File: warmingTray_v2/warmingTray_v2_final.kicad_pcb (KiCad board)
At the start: 2 copper layers, 116.1 x 53.8 mm, 38 parts, among them J1 Jack-DC, P1 Power, P2 Analog, P3 Analog, P4 Digital, P5 PWM, P6 PWM, P7 Communication

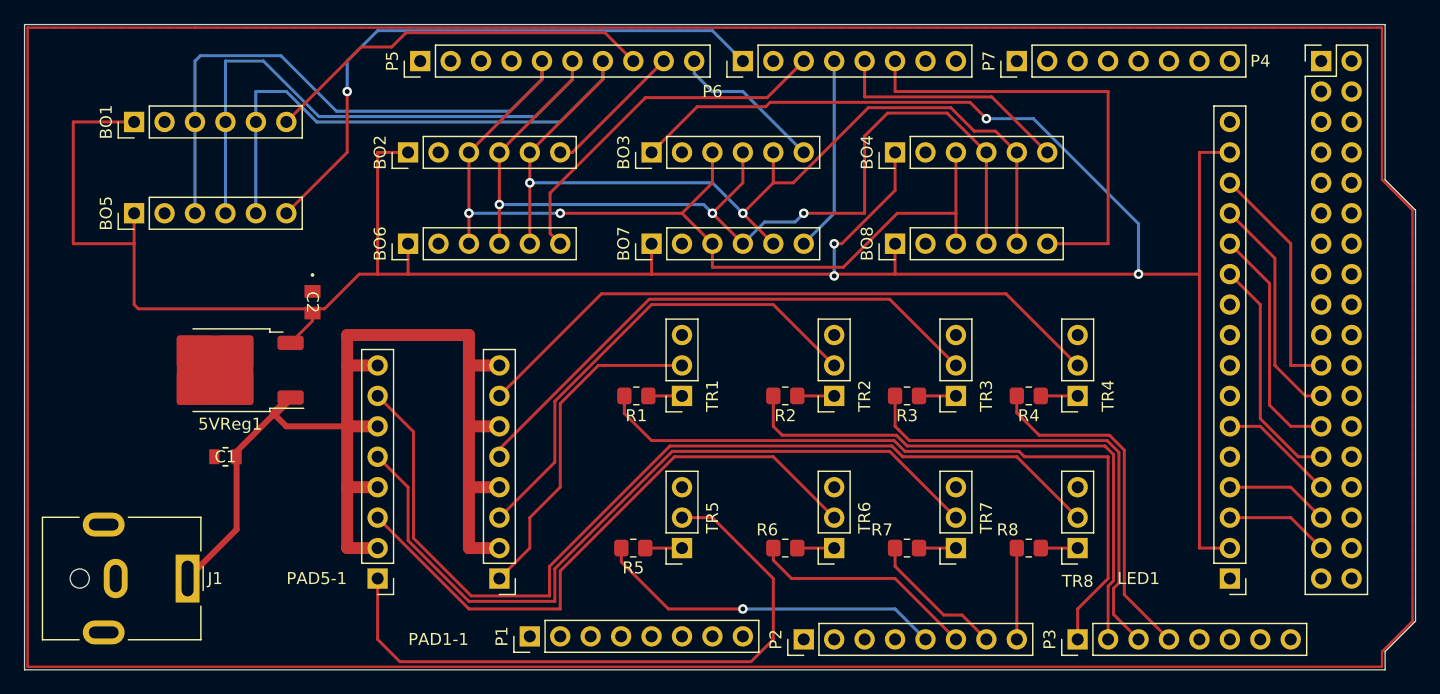
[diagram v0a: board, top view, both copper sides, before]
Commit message: PCB & Code
PCB: added 0805 footprints for resistors and capacitors
Code: testing controllers again so gains are being changed
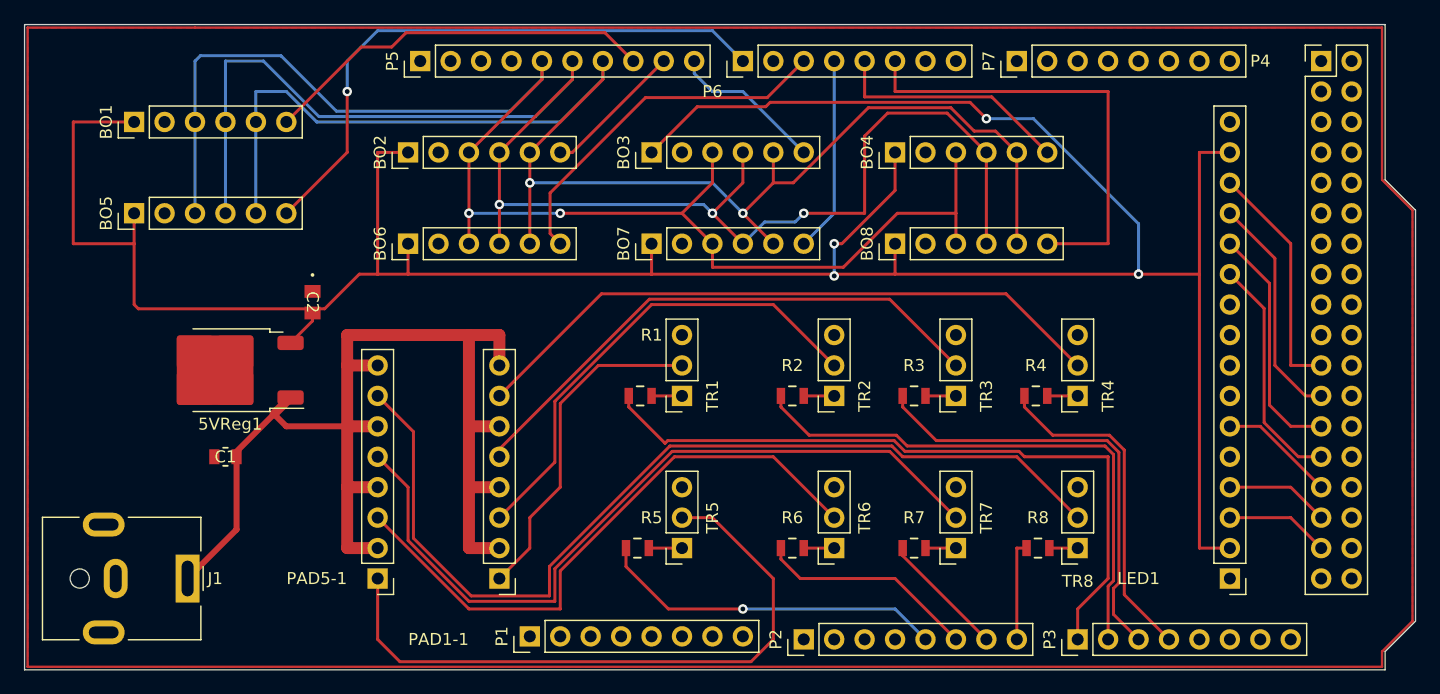
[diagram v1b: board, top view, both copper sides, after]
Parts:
- R1, R2, R3, R4, R5, R6, R7, R8: footprint Resistor_SMD:R_0805_2012Metric_Pad1.20x1.40mm_HandSolder -> footprints:RES_RK73G2A_KOA
- moved R8 0.77 mm to (184.6, 111.8)
- moved R2 0.59 mm to (164.1, 99.1)
- moved R3 0.59 mm to (174.3, 99.1)
- moved R4 0.59 mm to (184.5, 99.1)
- moved R6 0.59 mm to (164.1, 111.8)
- moved R7 0.59 mm to (174.3, 111.8)
- moved R5 0.34 mm to (151.2, 111.8)
- moved R1 0.32 mm to (151.4, 99.1)
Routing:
- net +12V: track 91.2 -> 93.8 mm
- net /A10: track 38.8 -> 37.2 mm
- net /A9: track 47.5 -> 45.9 mm
- net /A6: track 11.7 -> 10.5 mm
- net /A11: track 29.0 -> 28.1 mm
- net /A7: track 7.62 -> 8.43 mm
- net Net-(TR8-Pin_1): track 3.08 -> 2.36 mm
- net /A5: track 19.0 -> 18.3 mm
- net Net-(TR7-Pin_1): track 3.08 -> 2.54 mm
- net Net-(TR4-Pin_1): track 3.08 -> 2.54 mm
- net Net-(TR3-Pin_1): track 3.08 -> 2.54 mm
- net Net-(TR2-Pin_1): track 3.08 -> 2.54 mm
